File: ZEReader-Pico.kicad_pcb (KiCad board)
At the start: 2 copper layers, 110 x 110 mm, 85 parts, among them J1 Micro_SD_Card_Det2, J2 UART, J3 SWD, J4 USB4105-GF-A, J6 Conn_01x02_Socket, J7 FFC2B28-24-G, Q1 Si1308EDL, Q2 DMG2305UX-7, SW1 SW_Push, SW2 SW_Push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

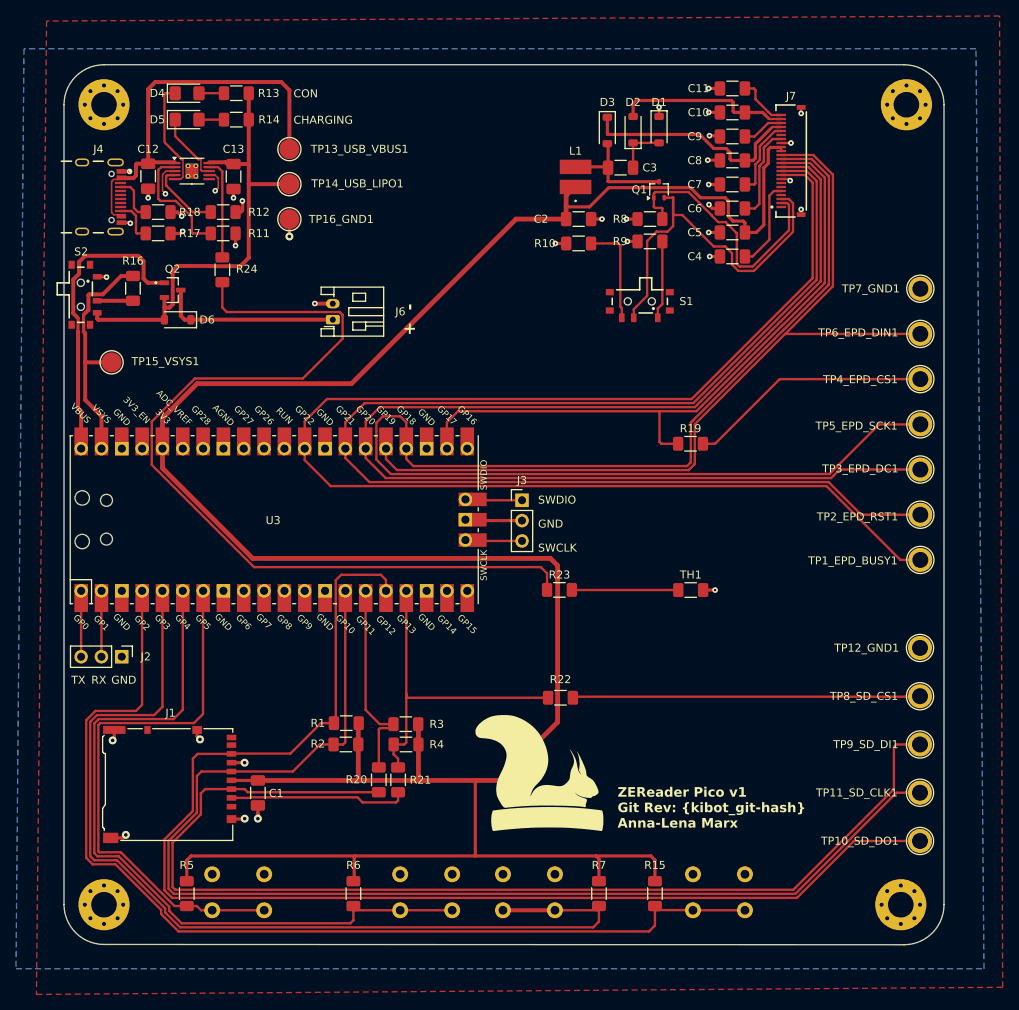
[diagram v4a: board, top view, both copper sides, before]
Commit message: Migrate to KiCad 9, start working on the new revision
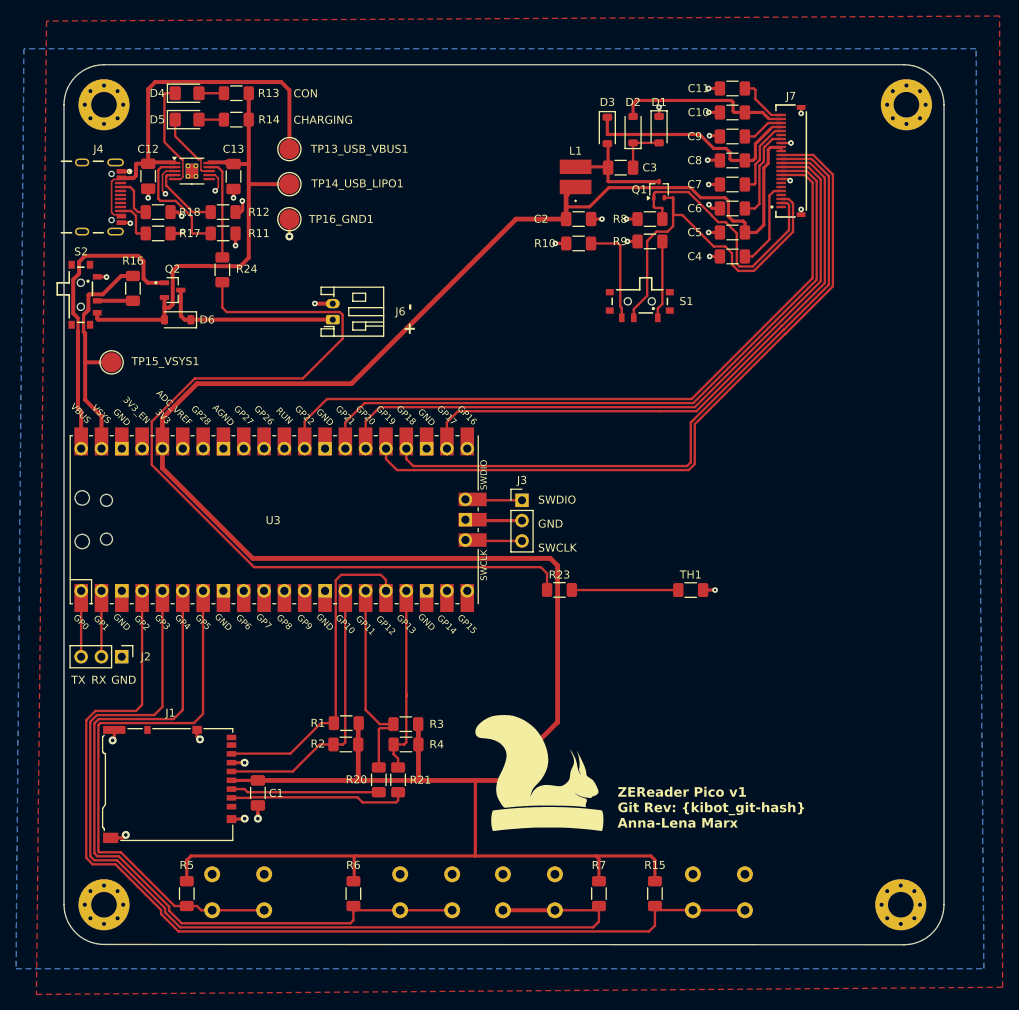
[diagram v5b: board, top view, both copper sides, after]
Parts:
- removed R19, R22: 0Ohm, Resistor_SMD:R_1206_3216Metric_Pad1.30x1.75mm_HandSolder
- removed REF**: KiCad-Logo2_6mm_SilkScreen, Symbol:KiCad-Logo2_6mm_SilkScreen
- removed TP10_SD_DO1: SD_DO, TestPoint:TestPoint_Plated_Hole_D2.0mm
- removed TP11_SD_CLK1: SD_SCLK, TestPoint:TestPoint_Plated_Hole_D2.0mm
- removed TP12_GND1, TP7_GND1: GND, TestPoint:TestPoint_Plated_Hole_D2.0mm
- removed TP1_EPD_BUSY1: EPD_BUSY, TestPoint:TestPoint_Plated_Hole_D2.0mm
- removed TP2_EPD_RST1: EPD_RST, TestPoint:TestPoint_Plated_Hole_D2.0mm
- removed TP3_EPD_DC1: EPD_DC, TestPoint:TestPoint_Plated_Hole_D2.0mm
- removed TP4_EPD_CS1: EPD_CS, TestPoint:TestPoint_Plated_Hole_D2.0mm
- removed TP5_EPD_SCK1: EPD_SCK, TestPoint:TestPoint_Plated_Hole_D2.0mm
- removed TP6_EPD_DIN1: EPD_DIN, TestPoint:TestPoint_Plated_Hole_D2.0mm
- removed TP8_SD_CS1: SD_CS, TestPoint:TestPoint_Plated_Hole_D2.0mm
- removed TP9_SD_DI1: SD_DI, TestPoint:TestPoint_Plated_Hole_D2.0mm
- C10, C11, C4, C5, C7, C8, C9: value 10uF -> 1uF
- R11: value 2.7k -> 1.5k
- renumbered SW4 to SW1, SW3 to SW2, SW2 to SW3, SW1 to SW4
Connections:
- net BTN_1 renamed /01_MCU/BTN_1
- net BTN_2 renamed /01_MCU/BTN_2
- net BTN_3 renamed /01_MCU/BTN_3
- net BTN_4 renamed /01_MCU/BTN_4
- net EPD_BUSY renamed /01_MCU/EPD_BUSY
- net EPD_CS renamed /01_MCU/EPD_CS
- net EPD_DC renamed /01_MCU/EPD_DC
- net EPD_DIN renamed /01_MCU/EPD_DIN
- net EPD_RST renamed /01_MCU/EPD_RST
- net EPD_SCK renamed /01_MCU/EPD_SCK
- net SD_CLK-SCLK renamed /01_MCU/SD_CLK-SCLK
- net SD_CMD-DI renamed /01_MCU/SD_CMD-DI
- net SD_DAT0-DO renamed /01_MCU/SD_DAT0-DO
- net SD_DAT3-CD-CS renamed /01_MCU/SD_DAT3-CD-CS
- net VBUS renamed /01_MCU/VBUS
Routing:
- net /01_MCU/SD_CMD-DI: track 165.7 -> 44.3 mm
- net /01_MCU/SD_DAT0-DO: track 161.5 -> 40.7 mm
- net /01_MCU/SD_CLK-SCLK: track 154.2 -> 34.7 mm
- net /01_MCU/EPD_SCK: track 170.8 -> 87.2 mm
- net /01_MCU/EPD_BUSY: track 174.1 -> 90.6 mm
- net /01_MCU/EPD_RST: track 162.8 -> 86.9 mm
- net /01_MCU/EPD_DC: track 157.8 -> 85.9 mm
- net Net-(R22-Pad2): track 43.3 -> 0.00 mm
- net Net-(R19-Pad2): track 30.5 -> 0.00 mm
- net /01_MCU/SD_DAT3-CD-CS: track 41.8 -> 24.1 mm
- net /01_MCU/EPD_DIN: track 108.5 -> 91.6 mm
- net /01_MCU/EPD_CS: track 83.4 -> 77.1 mm

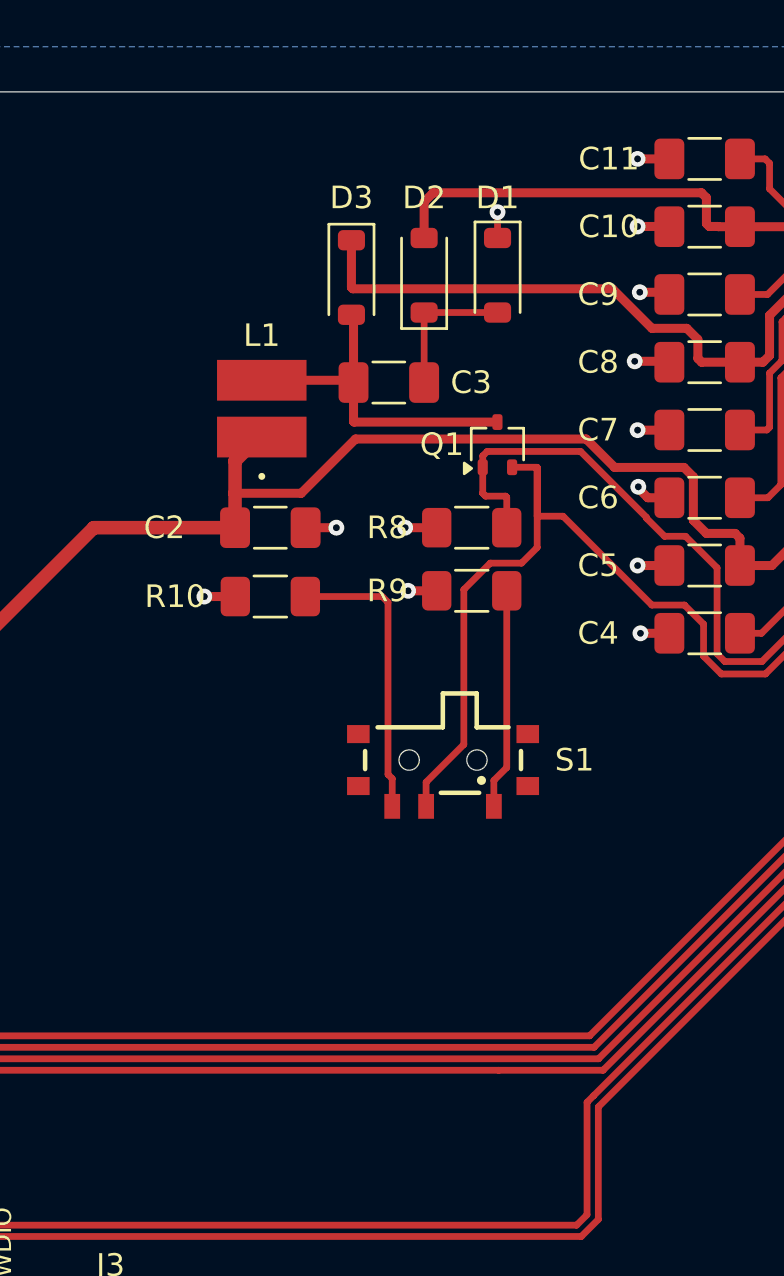
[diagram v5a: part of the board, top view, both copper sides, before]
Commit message: reworked epaper-driver schematic - corrected inverted ffc adapter
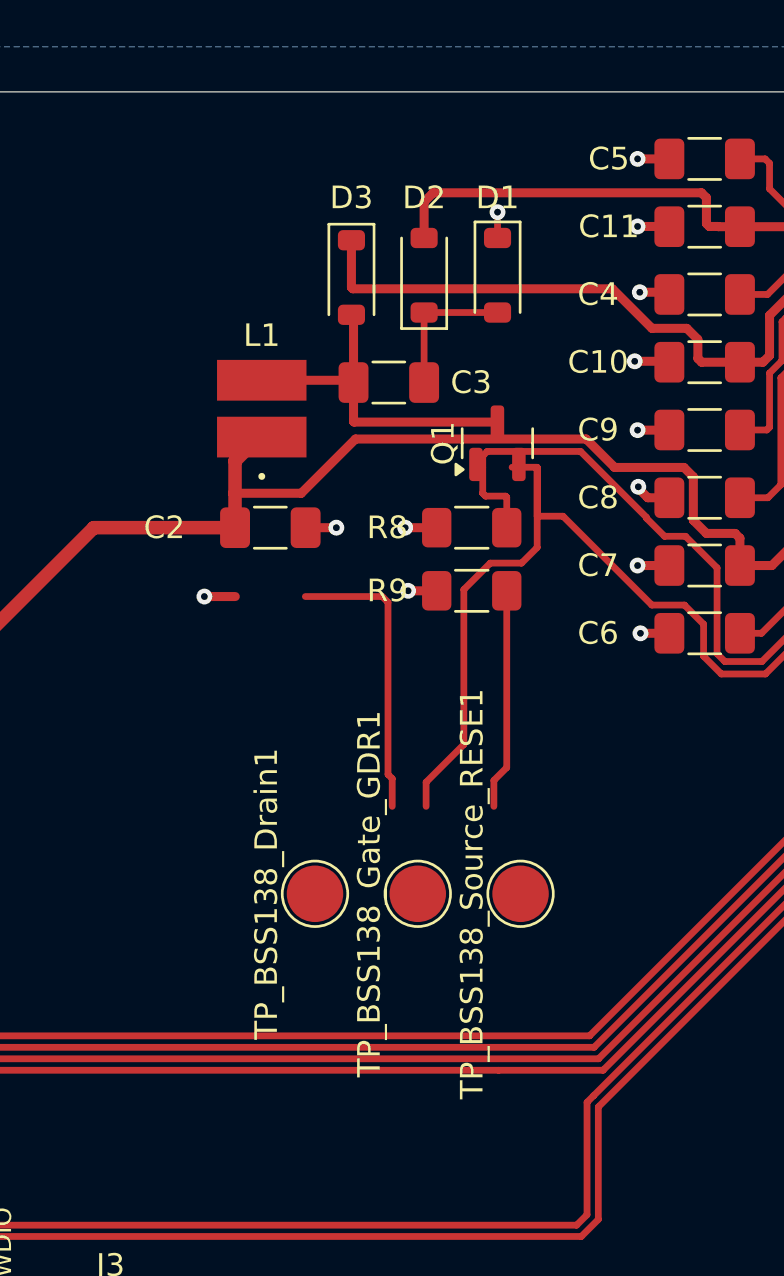
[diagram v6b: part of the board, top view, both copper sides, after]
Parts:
- removed R10: 3, Resistor_SMD:R_1206_3216Metric_Pad1.30x1.75mm_HandSolder
- removed S1: 450404015514, prj-footprints:450404015514
- added TP_BSS138_Drain1: BSS138_Drain, TestPoint:TestPoint_Pad_D2.5mm, F.Cu at (166.4, 75.5)
- added TP_BSS138_Gate_GDR1: BSS138_Gate, TestPoint:TestPoint_Pad_D2.5mm, F.Cu at (170.9, 75.5)
- added TP_BSS138_Source_RESE1: BSS138_Source, TestPoint:TestPoint_Pad_D2.5mm, F.Cu at (175.5, 75.5)
- C10: renamed from C8; value 1uF -> 1uF/25V
- C11: renamed from C10; value 1uF -> 1uF/50V
- C3: value 10uF -> 10uF/25V
- C4: renamed from C9; value 1uF -> 1uF/25V
- C5: renamed from C11; value 1uF -> 1uF/25V
- C6: renamed from C4; value 1uF -> 1uF/25V
- C7: renamed from C5; value 1uF -> 10uF/10V
- C8: renamed from C6; value 10uF -> 1uF/10V
- C9: renamed from C7; value 1uF -> 1uF/25V
- Q1: value Si1308EDL -> BSS138; footprint Package_TO_SOT_SMD:SOT-323_SC-70 -> Package_TO_SOT_SMD:SOT-23
- moved Q1 0.06 mm to (174.5, 55.6)
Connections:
- net Net-(D3-A) renamed /03_ePaper-Driver/Drain
- C10 pad 2: /03_ePaper-Driver/VGH -> Net-(C10-Pad2)
- C11 pad 2: /03_ePaper-Driver/VGL -> Net-(C11-Pad2)
- C4 pad 1: GND -> /03_ePaper-Driver/VGH
- C4 pad 2: Net-(C9-Pad2) -> GND
- C5 pad 1: GND -> /03_ePaper-Driver/VGL
- C5 pad 2: Net-(C11-Pad2) -> GND
- C6 pad 2: Net-(C4-Pad2) -> Net-(C6-Pad2)
- C8 pad 2: Net-(C6-Pad2) -> Net-(C8-Pad2)
- C9 pad 2: Net-(C7-Pad2) -> Net-(C9-Pad2)
- J7 pad 1: unconnected-(J7-Pad1) -> Net-(C11-Pad2)
- J7 pad 10: /01_MCU/EPD_RST -> +3.3V
- J7 pad 11: /01_MCU/EPD_DC -> /01_MCU/EPD_DIN
- J7 pad 12: /01_MCU/EPD_CS -> /01_MCU/EPD_SCK
- J7 pad 13: /01_MCU/EPD_SCK -> /01_MCU/EPD_CS
- J7 pad 14: /01_MCU/EPD_DIN -> /01_MCU/EPD_DC
- J7 pad 15: +3.3V -> /01_MCU/EPD_RST
- J7 pad 16: +3.3V -> /01_MCU/EPD_BUSY
- J7 pad 18: Net-(C6-Pad2) -> unconnected-(J7-Pad18)
- J7 pad 2: /03_ePaper-Driver/GDR -> /03_ePaper-Driver/VGL
- J7 pad 20: Net-(C7-Pad2) -> Net-(C6-Pad2)
- J7 pad 21: /03_ePaper-Driver/VGH -> unconnected-(J7-Pad21)
- J7 pad 22: Net-(C9-Pad2) -> /03_ePaper-Driver/RESE
- J7 pad 23: /03_ePaper-Driver/VGL -> /03_ePaper-Driver/GDR
- J7 pad 24: Net-(C11-Pad2) -> unconnected-(J7-Pad24)
- J7 pad 3: /03_ePaper-Driver/RESE -> Net-(C10-Pad2)
- J7 pad 4: unconnected-(J7-Pad4) -> /03_ePaper-Driver/VGH
- J7 pad 5: Net-(C4-Pad2) -> Net-(C9-Pad2)
- J7 pad 7: unconnected-(J7-Pad7) -> Net-(C8-Pad2)
- J7 pad 9: /01_MCU/EPD_BUSY -> +3.3V
- R9 pad 2: Net-(R9-Pad2) -> /03_ePaper-Driver/RESE
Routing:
- net (no net): track 0.00 -> 48.8 mm
- net Net-(C10-Pad2): track 0.00 -> 47.1 mm
- net /03_ePaper-Driver/RESE: track 47.1 -> 9.78 mm
- net /03_ePaper-Driver/Drain: track 15.1 -> 0.00 mm
- net Net-(R10-Pad1): track 12.9 -> 0.00 mm
- net Net-(C4-Pad2): track 11.1 -> 0.00 mm
- net Net-(R9-Pad2): track 9.78 -> 0.00 mm
- net Net-(C7-Pad2): track 9.71 -> 0.00 mm
- net Net-(C11-Pad2): track 6.56 -> 0.00 mm
- net GND: track 65.0 -> 68.8 mm, vias 37 -> 35
- net /03_ePaper-Driver/VGL: track 21.9 -> 23.3 mm, vias 0 -> 1
- net /03_ePaper-Driver/VGH: track 28.5 -> 29.8 mm, vias 0 -> 1

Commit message: switch to KiCad Pico extended symbol
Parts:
- removed U3: Pico, prj-footprints:RPi_Pico_SMD_TH
- added A1: RaspberryPi_Pico, Module:RaspberryPi_Pico_SMD, F.Cu at (126.4, 97.7)
- C2: value 10uF -> 4.7uF
- C3: value 10uF/25V -> 4.7uF
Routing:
- net +3.3V: track 327.1 -> 504.6 mm
- net /01_MCU/EPD_BUSY: track 90.6 -> 0.00 mm
- net /01_MCU/EPD_RST: track 86.9 -> 0.00 mm
- net /01_MCU/EPD_SCK: track 87.2 -> 77.1 mm
- net /01_MCU/EPD_CS: track 77.1 -> 87.2 mm
- net /01_MCU/EPD_DIN: track 91.6 -> 85.9 mm
- net /01_MCU/EPD_DC: track 85.9 -> 91.6 mm

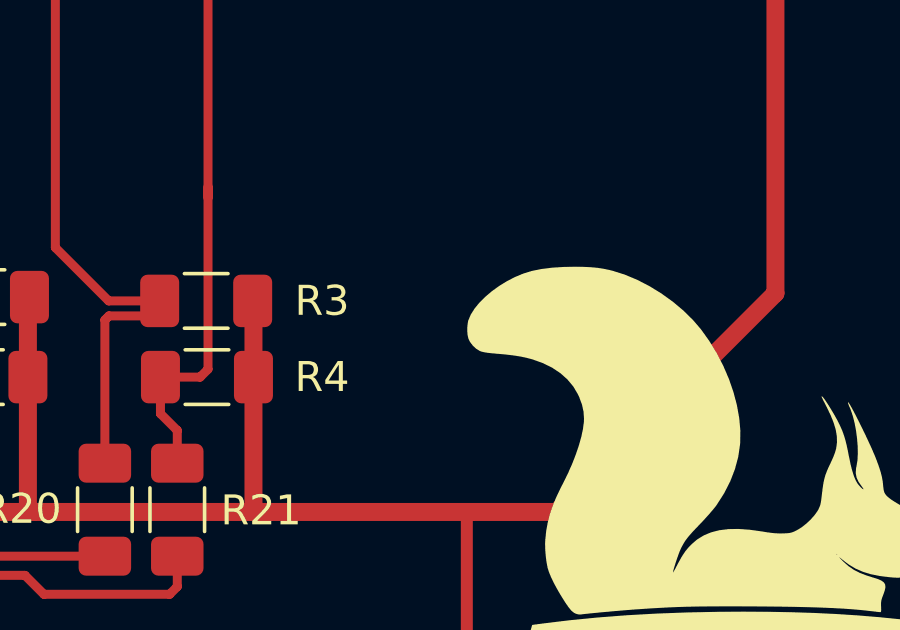
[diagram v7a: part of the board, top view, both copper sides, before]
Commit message: fully connect the sd connector, redraw sd and buttons
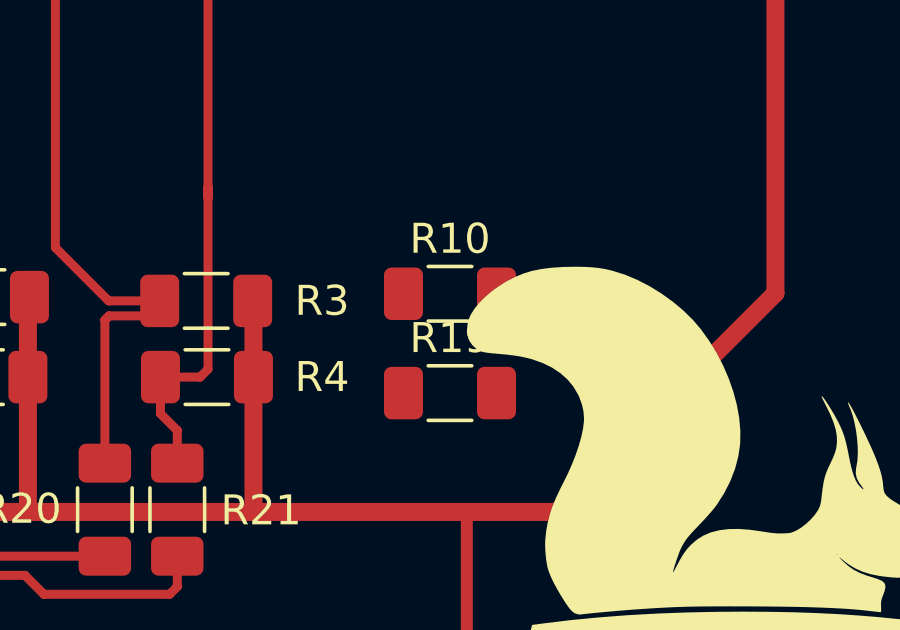
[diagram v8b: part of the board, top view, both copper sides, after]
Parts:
- added R10: 22k, Resistor_SMD:R_1206_3216Metric_Pad1.30x1.75mm_HandSolder, F.Cu at (150.9, 122.2)
- added R19: 22k, Resistor_SMD:R_1206_3216Metric_Pad1.30x1.75mm_HandSolder, F.Cu at (150.9, 125.5)
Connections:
- A1 pad 10: unconnected-(A1-GPIO7-Pad10) -> /01_MCU/SD_DET_B
- A1 pad 11: unconnected-(A1-GPIO8-Pad11) -> /01_MCU/SD_DAT1
- A1 pad 12: unconnected-(A1-GPIO9-Pad12) -> /01_MCU/SD_DAT2
- A1 pad 9: unconnected-(A1-GPIO6-Pad9) -> /01_MCU/SD_DET_A
- J1 pad 1: unconnected-(J1-DAT2-Pad1) -> /01_MCU/SD_DAT2
- J1 pad 10: unconnected-(J1-DET_A-Pad10) -> /01_MCU/SD_DET_A
- J1 pad 3: /01_MCU/SD_CMD-DI -> Net-(J1-CMD)
- J1 pad 8: unconnected-(J1-DAT1-Pad8) -> /01_MCU/SD_DAT1
- J1 pad 9: unconnected-(J1-DET_B-Pad9) -> /01_MCU/SD_DET_B
- R20 pad 1: /01_MCU/SD_CMD-DI -> Net-(J1-CMD)
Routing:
- net Net-(J1-CMD): track 0.00 -> 18.6 mm
- net /01_MCU/SD_CMD-DI: track 44.3 -> 25.8 mm
